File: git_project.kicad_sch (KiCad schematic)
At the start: 5 parts

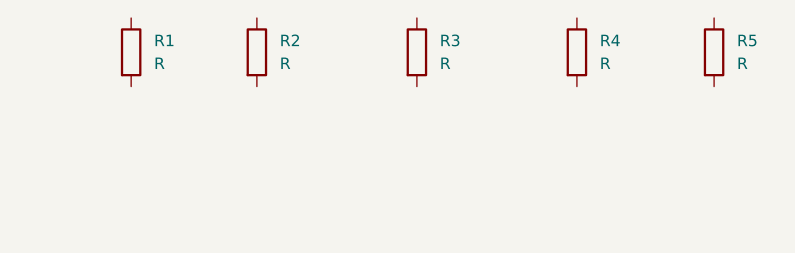
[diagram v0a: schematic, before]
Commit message: Capacitors Added.
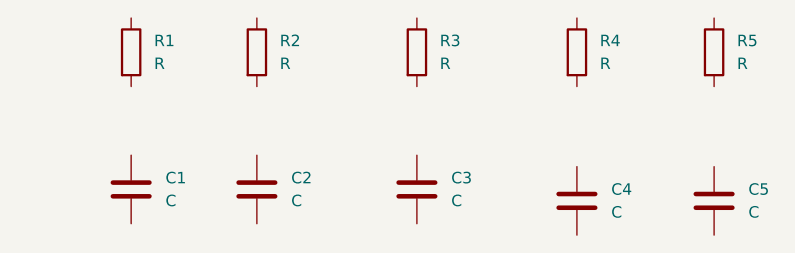
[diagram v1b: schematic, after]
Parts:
- added C1, C2, C3, C4, C5: C, symbol Device:C

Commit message: Added R6.
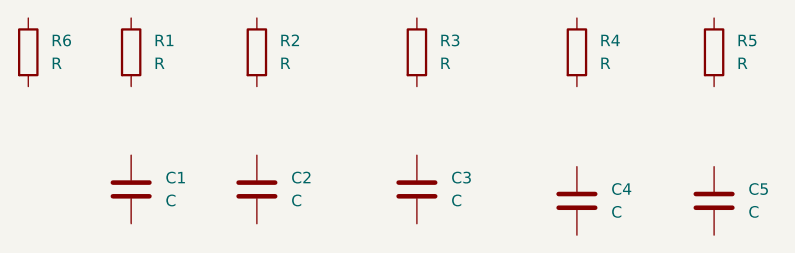
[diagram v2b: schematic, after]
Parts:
- added R6: R, symbol Device:R
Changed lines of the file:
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@@
+	)
+	(symbol
+		(lib_id "Device:R")
+		(at 71.12 101.6 0)
+		(unit 1)
+		(exclude_from_sim no)
+		(in_bom yes)
+		(on_board yes)
+		(dnp no)
+		(fields_autoplaced yes)
+		(property "Reference" "R6"
+			(at 73.66 100.3299 0)
+			(effects
+				(font
+					(size 1.27 1.27)
+				)
+				(justify left)
+			)
+		)
+		(property "Value" "R"
+			(at 73.66 102.8699 0)
+			(effects
+				(font
+					(size 1.27 1.27)
+				)
+				(justify left)
+			)
+		)
+		(property "Footprint" ""
+			(at 69.342 101.6 90)
+			(effects
+				(font
+					(size 1.27 1.27)
+				)
+				(hide yes)
+			)
+		)
+		(property "Datasheet" "~"
+			(at 71.12 101.6 0)
+			(effects
+				(font
+					(size 1.27 1.27)
+				)
+				(hide yes)
+			)
+		)
+		(property "Description" "Resistor"
+			(at 71.12 101.6 0)
+			(effects
+				(font
+					(size 1.27 1.27)
+				)
+				(hide yes)
+			)
+		)
+		(pin "1"
+		)
+		(pin "2"
+		)
+		(instances
+			(project "git_project"
+				(path "/001d275d-8048-4d2d-a133-97f829563c07"
+					(reference "R6")
+					(unit 1)
+				)
+			)
+		)
 	)
 	(symbol
